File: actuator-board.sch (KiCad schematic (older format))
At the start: 27 parts, among them U1 STM32F302K8U6, U2 MCP1703, U3 MAX3051, X1 16MHz 10ppm

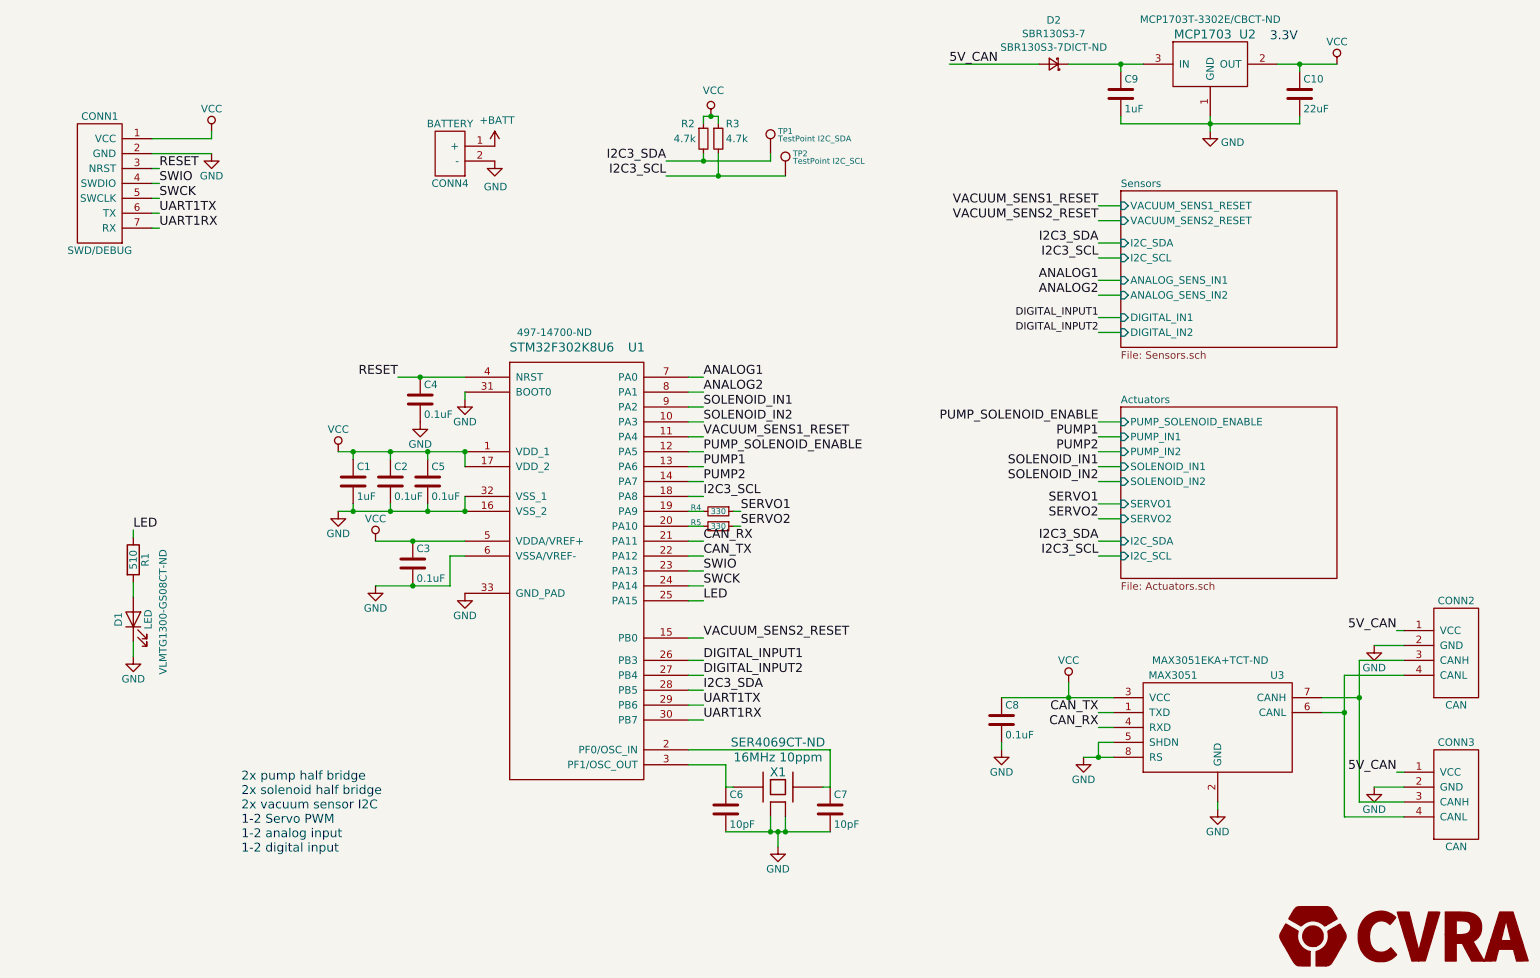
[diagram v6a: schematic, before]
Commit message: Clear component annotation
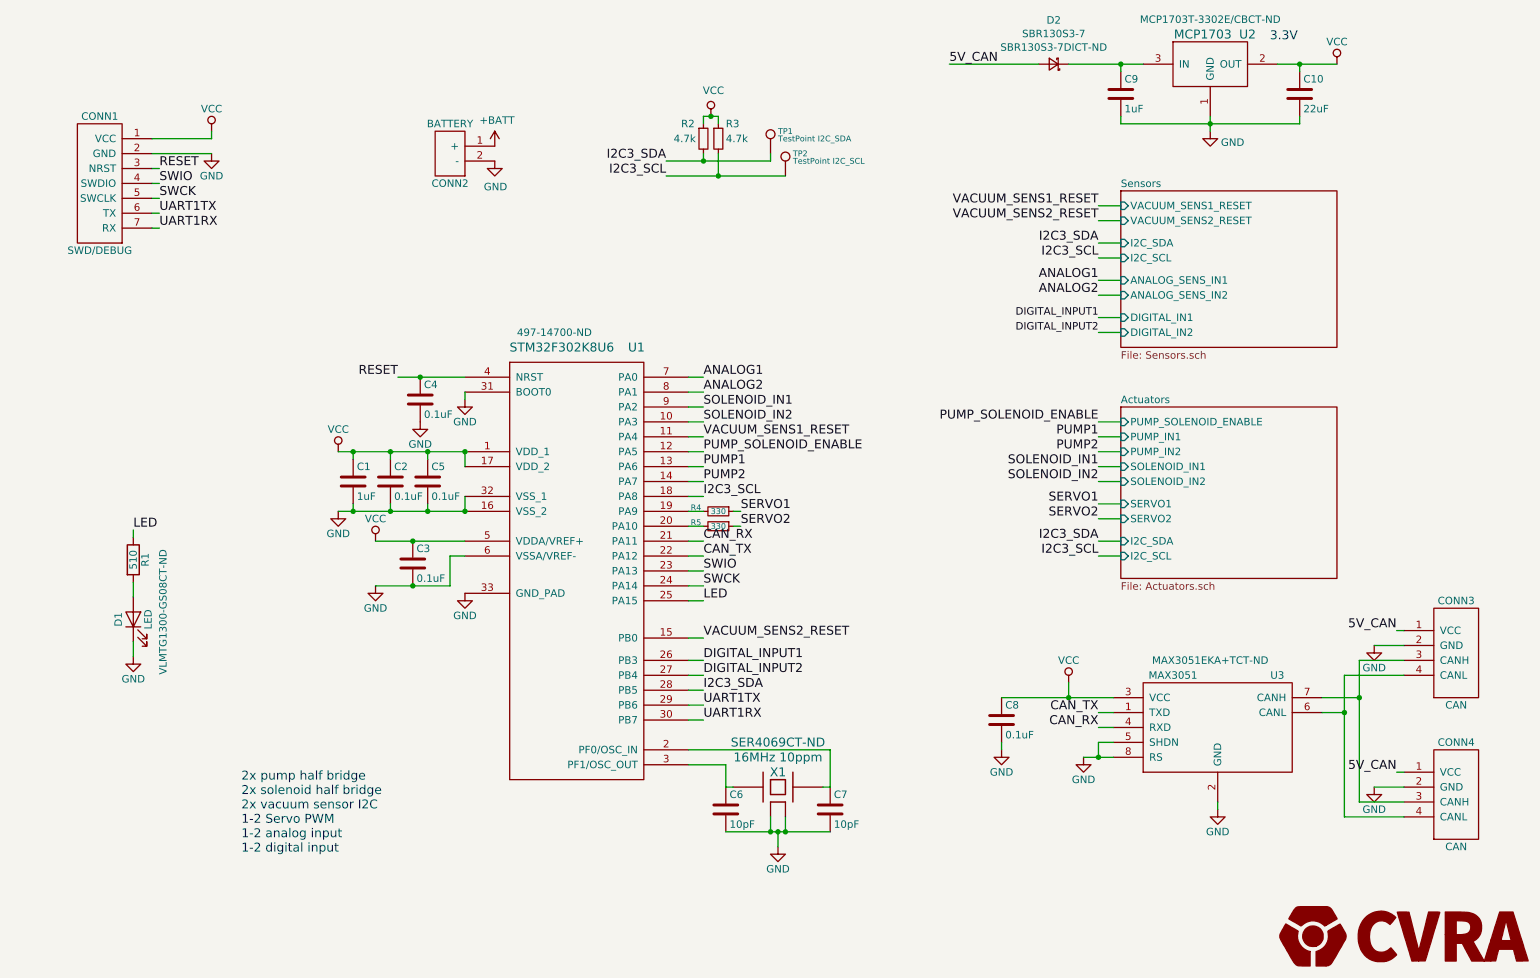
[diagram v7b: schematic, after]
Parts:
- renumbered CONN4 to CONN2, CONN2 to CONN3, CONN3 to CONN4
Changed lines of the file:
@@
 $EndComp
 $Comp
-L _connectors:CAN CONN2
+L _connectors:CAN CONN3
 U 1 1 56D60A8A
 P 10500 4950
-F 0 "CONN2" H 10500 5300 50  0000 C CNN
+F 0 "CONN3" H 10500 5300 50  0000 C CNN
 F 1 "CAN" H 10500 4600 50  0000 C CNN
 F 2 "Connector_Molex:Molex_PicoBlade_53261-0471_1x04-1MP_P1.25mm_Horizontal" H 10750 4950 50  0001 C CNN
@@
 $EndComp
 $Comp
-L _connectors:CAN CONN3
+L _connectors:CAN CONN4
 U 1 1 56D60AB3
 P 10500 5900
-F 0 "CONN3" H 10500 6250 50  0000 C CNN
+F 0 "CONN4" H 10500 6250 50  0000 C CNN
 F 1 "CAN" H 10500 5550 50  0000 C CNN
 F 2 "Connector_Molex:Molex_PicoBlade_53261-0471_1x04-1MP_P1.25mm_Horizontal" H 10750 5900 50  0001 C CNN
@@
 5V_CAN
 $Comp
-L power:GND #PWR02
+L power:GND #PWR021
 U 1 1 56D60E25
 P 9950 4900
-F 0 "#PWR02" H 9950 4650 50  0001 C CNN
+F 0 "#PWR021" H 9950 4650 50  0001 C CNN
 F 1 "GND" H 9950 4750 50  0000 C CNN
 F 2 "" H 9950 4900 50  0000 C CNN
@@
 $EndComp
 $Comp
-L power:GND #PWR03
+L power:GND #PWR022
 U 1 1 56D60E6A
 P 9950 5850
-F 0 "#PWR03" H 9950 5600 50  0001 C CNN
+F 0 "#PWR022" H 9950 5600 50  0001 C CNN
 F 1 "GND" H 9950 5700 50  0000 C CNN
 F 2 "" H 9950 5850 50  0000 C CNN
@@
 CAN_RX
 $Comp
-L power:VCC #PWR05
+L power:VCC #PWR016
 U 1 1 56D61232
 P 7900 5150
-F 0 "#PWR05" H 7900 5000 50  0001 C CNN
+F 0 "#PWR016" H 7900 5000 50  0001 C CNN
 F 1 "VCC" H 7900 5300 50  0000 C CNN
 F 2 "" H 7900 5150 50  0000 C CNN
@@
 $EndComp
 $Comp
-L power:GND #PWR06
+L power:GND #PWR015
 U 1 1 56D612E3
 P 7450 5600
-F 0 "#PWR06" H 7450 5350 50  0001 C CNN
+F 0 "#PWR015" H 7450 5350 50  0001 C CNN
 F 1 "GND" H 7450 5450 50  0000 C CNN
 F 2 "" H 7450 5600 50  0000 C CNN
@@
 $EndComp
 $Comp
-L power:GND #PWR07
+L power:GND #PWR019
 U 1 1 56D61353
 P 8900 6000
-F 0 "#PWR07" H 8900 5750 50  0001 C CNN
+F 0 "#PWR019" H 8900 5750 50  0001 C CNN
 F 1 "GND" H 8900 5850 50  0000 C CNN
 F 2 "" H 8900 6000 50  0000 C CNN
@@
 $EndComp
 $Comp
-L power:GND #PWR09
+L power:GND #PWR03
 U 1 1 56D62F04
 P 2150 1600
-F 0 "#PWR09" H 2150 1350 50  0001 C CNN
+F 0 "#PWR03" H 2150 1350 50  0001 C CNN
 F 1 "GND" H 2150 1450 50  0000 C CNN
 F 2 "" H 2150 1600 50  0000 C CNN
@@
 RESET
 $Comp
-L power:GND #PWR010
+L power:GND #PWR09
 U 1 1 56D634B2
 P 3850 3250
-F 0 "#PWR010" H 3850 3000 50  0001 C CNN
+F 0 "#PWR09" H 3850 3000 50  0001 C CNN
 F 1 "GND" H 3850 3100 50  0000 C CNN
 F 2 "" H 3850 3250 50  0000 C CNN
@@
 $EndComp
 $Comp
-L power:GND #PWR011
+L power:GND #PWR08
 U 1 1 56D636C6
 P 3550 3400
-F 0 "#PWR011" H 3550 3150 50  0001 C CNN
+F 0 "#PWR08" H 3550 3150 50  0001 C CNN
 F 1 "GND" H 3550 3250 50  0000 C CNN
 F 2 "" H 3550 3400 50  0000 C CNN
@@
 $EndComp
 $Comp
-L power:GND #PWR012
+L power:GND #PWR014
 U 1 1 56D63CD1
 P 5950 6250
-F 0 "#PWR012" H 5950 6000 50  0001 C CNN
+F 0 "#PWR014" H 5950 6000 50  0001 C CNN
 F 1 "GND" H 5950 6100 50  0000 C CNN
 F 2 "" H 5950 6250 50  0000 C CNN
@@
 LED
 $Comp
-L power:VCC #PWR014
+L power:VCC #PWR04
 U 1 1 56D64703
 P 3000 3600
-F 0 "#PWR014" H 3000 3450 50  0001 C CNN
+F 0 "#PWR04" H 3000 3450 50  0001 C CNN
 F 1 "VCC" H 3000 3750 50  0000 C CNN
 F 2 "" H 3000 3600 50  0000 C CNN
@@
 $EndComp
 $Comp
-L power:VCC #PWR015
+L power:VCC #PWR06
 U 1 1 56D6474A
 P 3250 4200
-F 0 "#PWR015" H 3250 4050 50  0001 C CNN
+F 0 "#PWR06" H 3250 4050 50  0001 C CNN
 F 1 "VCC" H 3250 4350 50  0000 C CNN
 F 2 "" H 3250 4200 50  0000 C CNN
@@
 $EndComp
 $Comp
-L power:GND #PWR016
+L power:GND #PWR07
 U 1 1 56D64793
 P 3250 4500
-F 0 "#PWR016" H 3250 4250 50  0001 C CNN
+F 0 "#PWR07" H 3250 4250 50  0001 C CNN
 F 1 "GND" H 3250 4350 50  0000 C CNN
 F 2 "" H 3250 4500 50  0000 C CNN
@@
 $EndComp
 $Comp
-L power:GND #PWR017
+L power:GND #PWR05
 U 1 1 56D64969
 P 3000 4000
-F 0 "#PWR017" H 3000 3750 50  0001 C CNN
+F 0 "#PWR05" H 3000 3750 50  0001 C CNN
 F 1 "GND" H 3000 3850 50  0000 C CNN
 F 2 "" H 3000 4000 50  0000 C CNN
@@
 	9850 5250 9850 5950
 $Comp
-L power:GND #PWR020
+L power:GND #PWR010
 U 1 1 5BC69DE1
 P 3850 4550
-F 0 "#PWR020" H 3850 4300 50  0001 C CNN
+F 0 "#PWR010" H 3850 4300 50  0001 C CNN
 F 1 "GND" H 3850 4400 50  0000 C CNN
 F 2 "" H 3850 4550 50  0000 C CNN
@@
 $EndComp
 $Comp
-L power:GND #PWR0101
+L power:GND #PWR017
 U 1 1 5BCD4843
 P 8000 5650
-F 0 "#PWR0101" H 8000 5400 50  0001 C CNN
+F 0 "#PWR017" H 8000 5400 50  0001 C CNN
 F 1 "GND" H 8000 5500 50  0000 C CNN
 F 2 "" H 8000 5650 50  0000 C CNN
@@
 	3550 3100 3850 3100
 $Comp
-L power:GND #PWR01
+L power:GND #PWR018
 U 1 1 56D60C84
 P 8850 1450
-F 0 "#PWR01" H 8850 1200 50  0001 C CNN
+F 0 "#PWR018" H 8850 1200 50  0001 C CNN
 F 1 "GND" H 9000 1375 50  0000 C CNN
 F 2 "" H 8850 1450 50  0000 C CNN
@@
 	8850 1400 9450 1400
 $Comp
-L power:VCC #PWR04
+L power:VCC #PWR020
 U 1 1 56D61015
 P 9700 1000
-F 0 "#PWR04" H 9700 850 50  0001 C CNN
+F 0 "#PWR020" H 9700 850 50  0001 C CNN
 F 1 "VCC" H 9700 1150 50  0000 C CNN
 F 2 "" H 9700 1000 50  0000 C CNN
@@
 VACUUM_SENS1_RESET
 $Comp
-L _connectors:PWR CONN4
+L _connectors:PWR CONN2
 U 1 1 5E236F0F
 P 3700 1600
-F 0 "CONN4" H 3650 1400 50  0000 C CNN
+F 0 "CONN2" H 3650 1400 50  0000 C CNN
 F 1 "BATTERY" H 3650 1800 50  0000 C CNN
 F 2 "MODULE" H 3950 1600 50  0001 C CNN
@@
 $EndComp
 $Comp
-L power:+BATT #PWR018
+L power:+BATT #PWR011
 U 1 1 5E237F12
 P 4050 1550
-F 0 "#PWR018" H 4050 1400 50  0001 C CNN
+F 0 "#PWR011" H 4050 1400 50  0001 C CNN
 F 1 "+BATT" H 4065 1723 50  0000 C CNN
 F 2 "" H 4050 1550 50  0001 C CNN
@@
 	3500 4500 3750 4500
 $Comp
-L power:GND #PWR0102
+L power:GND #PWR012
 U 1 1 5E2B5273
 P 4050 1650
-F 0 "#PWR0102" H 4050 1400 50  0001 C CNN
+F 0 "#PWR012" H 4050 1400 50  0001 C CNN
 F 1 "GND" H 4055 1477 50  0000 C CNN
 F 2 "" H 4050 1650 50  0001 C CNN
@@
 	2150 1500 2150 1450
 $Comp
-L power:VCC #PWR08
+L power:VCC #PWR02
 U 1 1 56D62E77
 P 2150 1450
-F 0 "#PWR08" H 2150 1300 50  0001 C CNN
+F 0 "#PWR02" H 2150 1300 50  0001 C CNN
 F 1 "VCC" H 2150 1600 50  0000 C CNN
 F 2 "" H 2150 1450 50  0000 C CNN
@@
 LED
 $Comp
-L power:GND #PWR013
+L power:GND #PWR01
 U 1 1 56D640B3
 P 1625 4975
-F 0 "#PWR013" H 1625 4725 50  0001 C CNN
+F 0 "#PWR01" H 1625 4725 50  0001 C CNN
 F 1 "GND" H 1625 4825 50  0000 C CNN
 F 2 "" H 1625 4975 50  0000 C CNN
@@
 $EndComp
 $Comp
-L power:VCC #PWR0103
+L power:VCC #PWR013
 U 1 1 5E2B5516
 P 5500 1350
-F 0 "#PWR0103" H 5500 1200 50  0001 C CNN
+F 0 "#PWR013" H 5500 1200 50  0001 C CNN
 F 1 "VCC" H 5517 1523 50  0000 C CNN
 F 2 "" H 5500 1350 50  0001 C CNN
